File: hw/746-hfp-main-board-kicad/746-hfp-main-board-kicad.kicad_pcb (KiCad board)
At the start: 2 copper layers, 140 x 90 mm, 59 parts, among them J1 5V, J10 Conn_01x01_Socket, J11 Conn_01x01_Socket, J12 Phone_Connector, J13 ESP32_Left_Pins, J14 ESP32_Right_Pins, J15 Power_Connector, J16 Control_board_Connector, J17 Control_board_connector, J18 Conn_01x01_Socket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

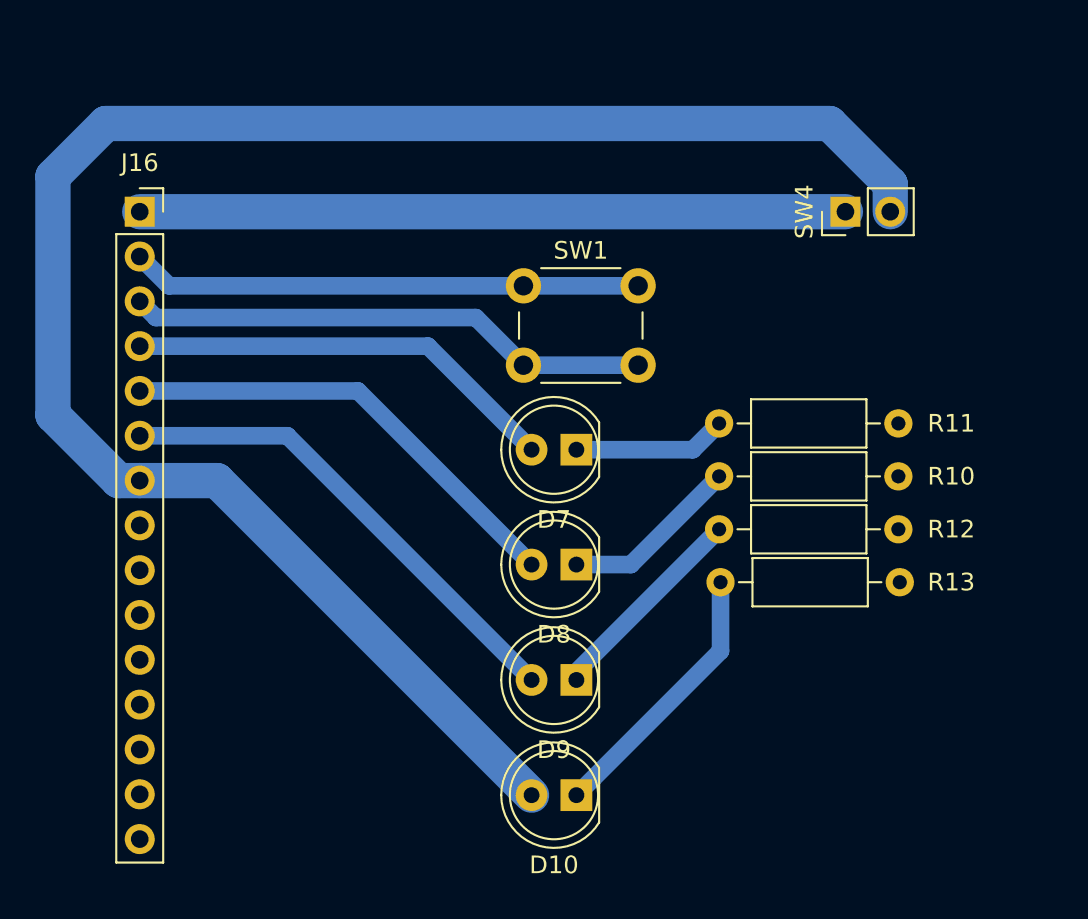
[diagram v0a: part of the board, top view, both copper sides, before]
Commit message: Add schematic & pcb for control board
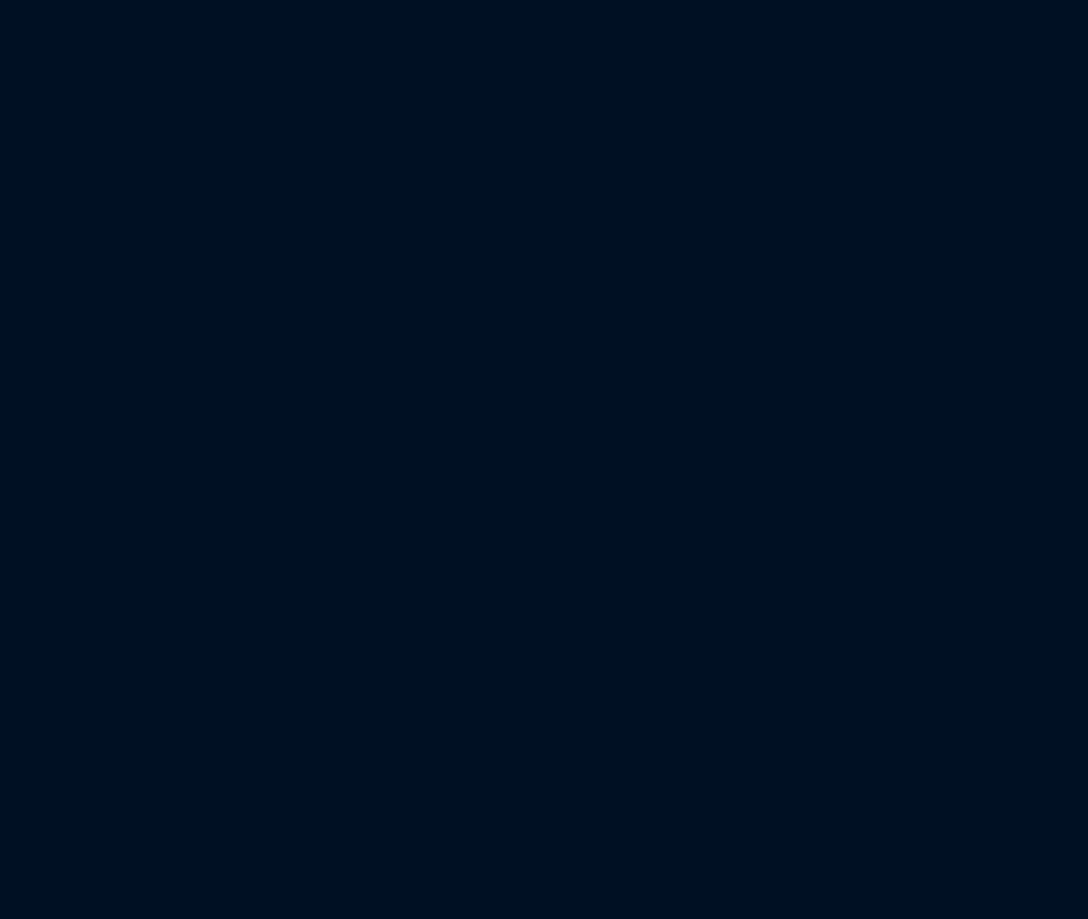
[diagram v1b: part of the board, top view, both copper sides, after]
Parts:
- removed D10, D7, D8, D9: LED, LED_THT:LED_D5.0mm
- removed J16: Control_board_Connector, Connector_PinSocket_2.54mm:PinSocket_1x15_P2.54mm_Vertical
- removed R10, R12: 220, Resistor_THT:R_Axial_DIN0207_L6.3mm_D2.5mm_P10.16mm_Horizontal
- removed R11: 2k, Resistor_THT:R_Axial_DIN0207_L6.3mm_D2.5mm_P10.16mm_Horizontal
- removed R13: 1k, Resistor_THT:R_Axial_DIN0207_L6.3mm_D2.5mm_P10.16mm_Horizontal
- removed SW1: SW_Push, Button_Switch_THT:SW_PUSH_6mm_H5mm
- removed SW4: SW_SPST, Connector_PinHeader_2.54mm:PinHeader_1x02_P2.54mm_Vertical
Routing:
- net +5V: track 276.9 -> 175.6 mm
- net /Control board/+5V_pre_switch: track 40.0 -> 0.00 mm
- net /Control board/ENABLE_PAIRING_BTN (18): track 29.7 -> 0.00 mm
- net /Control board/+3.3V: track 28.9 -> 0.00 mm
- net /Control board/HookSwitchOut (2): track 27.9 -> 0.00 mm
- net /Control board/RingerSignal (16): track 26.3 -> 0.00 mm
- net /Control board/BT_LED_STATE (19): track 24.6 -> 0.00 mm
- net Net-(D10-K): track 15.5 -> 0.00 mm
- net Net-(D9-K): track 11.9 -> 0.00 mm
- net Net-(D8-K): track 10.2 -> 0.00 mm
- net Net-(D7-K): track 8.71 -> 0.00 mm

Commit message: Create kicad pcb
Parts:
- C6: value 2.2nF -> 3.3nF
- J15: footprint Connector_PinHeader_2.54mm:PinHeader_1x02_P2.54mm_Vertical -> Connector_JST:JST_XH_B2B-XH-A_1x02_P2.50mm_Vertical
- R3: value 20k -> 10k
- moved J15 80.5 mm to (145.0, 69.0)
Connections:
- U3 pad 1: +3.3V_Clean -> Net-(U3-REF)
- U3 pad 2: (no net) -> GND
- U3 pad 3: (no net) -> +3.3V_Clean
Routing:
- net GNDA: track 109.4 -> 537.7 mm, vias 2 -> 4
- net +5V: track 175.6 -> 545.8 mm, vias 4 -> 5
- net Mic+: track 12.9 -> 201.7 mm
- net Speaker+: track 11.2 -> 194.0 mm
- net GND: track 0.00 -> 167.9 mm, vias 0 -> 4
- net RingerSignal (16): track 79.8 -> 135.6 mm
- net HookSwitchOut (2): track 25.2 -> 78.1 mm
- net Ringer+: track 9.65 -> 56.5 mm
- net +3.3V_Clean: track 63.8 -> 74.2 mm
- net +3.3V: track 96.2 -> 87.8 mm
- net HookSwitchPower (4): track 23.6 -> 30.2 mm
- net +5V_pre_switch: track 6.24 -> 9.22 mm, vias 1 -> 0
- net Pico_Enable: track 64.1 -> 66.3 mm
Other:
- board text added: "The board is not meant for manufacturing as such some DRC violations have been ignored. Front copper layer is routed only to fool DRC. The actual board is single sided and uses jumper wires acros vias"

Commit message: Improve kicad related
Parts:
- added REF**: PinSocket_1x01_P2.54mm_Vertical, Connector_PinSocket_2.54mm:PinSocket_1x01_P2.54mm_Vertical, F.Cu at (89.0, 29.0)
- added REF**: PinSocket_1x01_P2.54mm_Vertical, Connector_PinSocket_2.54mm:PinSocket_1x01_P2.54mm_Vertical, F.Cu at (95.0, 66.0)
- added REF**: PinSocket_1x01_P2.54mm_Vertical, Connector_PinSocket_2.54mm:PinSocket_1x01_P2.54mm_Vertical, F.Cu at (214.0, 67.0)
- added REF**: PinSocket_1x01_P2.54mm_Vertical, Connector_PinSocket_2.54mm:PinSocket_1x01_P2.54mm_Vertical, F.Cu at (129.0, 63.0)
- added REF**: PinSocket_1x01_P2.54mm_Vertical, Connector_PinSocket_2.54mm:PinSocket_1x01_P2.54mm_Vertical, F.Cu at (142.0, 79.0)
- added REF**: PinSocket_1x01_P2.54mm_Vertical, Connector_PinSocket_2.54mm:PinSocket_1x01_P2.54mm_Vertical, F.Cu at (191.0, 38.0)
- added REF**: PinSocket_1x01_P2.54mm_Vertical, Connector_PinSocket_2.54mm:PinSocket_1x01_P2.54mm_Vertical, F.Cu at (142.0, 74.0)
- added REF**: PinSocket_1x01_P2.54mm_Vertical, Connector_PinSocket_2.54mm:PinSocket_1x01_P2.54mm_Vertical, F.Cu at (115.0, 32.0)
- added REF**: PinSocket_1x01_P2.54mm_Vertical, Connector_PinSocket_2.54mm:PinSocket_1x01_P2.54mm_Vertical, F.Cu at (108.0, 41.0)
- added REF**: PinSocket_1x01_P2.54mm_Vertical, Connector_PinSocket_2.54mm:PinSocket_1x01_P2.54mm_Vertical, F.Cu at (150.0, 88.0)
- added REF**: PinSocket_1x01_P2.54mm_Vertical, Connector_PinSocket_2.54mm:PinSocket_1x01_P2.54mm_Vertical, F.Cu at (195.0, 30.0)
- added REF**: PinSocket_1x01_P2.54mm_Vertical, Connector_PinSocket_2.54mm:PinSocket_1x01_P2.54mm_Vertical, F.Cu at (192.0, 83.0)
- added REF**: PinSocket_1x01_P2.54mm_Vertical, Connector_PinSocket_2.54mm:PinSocket_1x01_P2.54mm_Vertical, F.Cu at (151.0, 66.0)
- added REF**: PinSocket_1x01_P2.54mm_Vertical, Connector_PinSocket_2.54mm:PinSocket_1x01_P2.54mm_Vertical, F.Cu at (156.0, 23.0)
- added REF**: PinSocket_1x01_P2.54mm_Vertical, Connector_PinSocket_2.54mm:PinSocket_1x01_P2.54mm_Vertical, F.Cu at (163.0, 106.0)
- added REF**: PinSocket_1x01_P2.54mm_Vertical, Connector_PinSocket_2.54mm:PinSocket_1x01_P2.54mm_Vertical, F.Cu at (113.0, 25.0)
- added REF**: PinSocket_1x01_P2.54mm_Vertical, Connector_PinSocket_2.54mm:PinSocket_1x01_P2.54mm_Vertical, F.Cu at (94.0, 43.0)
- added REF**: PinSocket_1x01_P2.54mm_Vertical, Connector_PinSocket_2.54mm:PinSocket_1x01_P2.54mm_Vertical, F.Cu at (171.0, 85.0)
- added REF**: PinSocket_1x01_P2.54mm_Vertical, Connector_PinSocket_2.54mm:PinSocket_1x01_P2.54mm_Vertical, F.Cu at (83.0, 30.0)
- added REF**: PinSocket_1x01_P2.54mm_Vertical, Connector_PinSocket_2.54mm:PinSocket_1x01_P2.54mm_Vertical, F.Cu at (102.0, 68.0)
- added REF**: PinSocket_1x01_P2.54mm_Vertical, Connector_PinSocket_2.54mm:PinSocket_1x01_P2.54mm_Vertical, F.Cu at (94.0, 38.0)
- added REF**: PinSocket_1x01_P2.54mm_Vertical, Connector_PinSocket_2.54mm:PinSocket_1x01_P2.54mm_Vertical, F.Cu at (116.0, 28.0)
- added REF**: PinSocket_1x01_P2.54mm_Vertical, Connector_PinSocket_2.54mm:PinSocket_1x01_P2.54mm_Vertical, F.Cu at (199.0, 59.0)
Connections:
- J12 pad 6: Dialer (15) -> HookSwitchOut (2)
- J14 pad 13: Dialer (15) -> HookSwitchOut (2)
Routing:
- net HookSwitchOut (2): track 78.1 -> 106.0 mm, vias 2 -> 0
- net Dialer (15): track 26.8 -> 0.00 mm
- net GND: track 167.9 -> 164.2 mm, vias 4 -> 0
- net RingerSignal (16): track 135.6 -> 138.4 mm, vias 2 -> 0
- net BT_LED_STATE (19): track 34.9 -> 37.0 mm
- net GNDA: track 537.7 -> 535.6 mm, vias 4 -> 0
- net ENABLE_PAIRING_BTN (18): track 35.2 -> 37.0 mm
- net +5V: track 545.8 -> 544.1 mm, vias 5 -> 0
- net Ringer+: track 56.5 -> 56.9 mm, vias 2 -> 0
- net Mic+: track 201.7 -> 201.6 mm, vias 2 -> 0
- net Speaker+: track 194.0 -> 193.9 mm, vias 2 -> 0
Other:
- board text added: "BUG: The spacing between the ESP32 pin rows is about 1.5mm smaller than it should. If you're planning to use this board, increase the spacing between J13 and J14"

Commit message: Fixed pcb
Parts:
- Q1: footprint Package_TO_SOT_THT:TO-220-3_Vertical -> Package_TO_SOT_THT:TO-92
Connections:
- J12 pad 6: HookSwitchOut (2) -> Dialer(15)
- J14 pad 13: HookSwitchOut (2) -> Dialer(15)
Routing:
- net Dialer(15): track 0.00 -> 27.2 mm
- net HookSwitchOut (2): track 106.0 -> 78.9 mm
- net GND: track 164.2 -> 175.9 mm
- net RingerEnabled (17): track 56.7 -> 61.3 mm
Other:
- board text added: "BUG: The spacing between the ESP32 pin rows is about 1.5mm smaller than it should be. If you're planning to use this board, increase the spacing between J13 and J14"
- board text removed: "BUG: The spacing between the ESP32 pin rows is about 1.5mm smaller than it should. If you're planning to use this board, increase the spacing between J13 and J14"

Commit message: Fixed board
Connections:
- net Dialer(15) renamed Dialer (15)
- J13 pad 10: unconnected-(J13-Pin_10-Pad10) -> Audio_SCL (27)
- J13 pad 8: Audio_SCL (27) -> unconnected-(J13-Pin_8-Pad8)
- U3 pad 1: Net-(U3-REF) -> +3.3V_Clean
- U3 pad 2: GND -> (no net)
- U3 pad 3: +3.3V_Clean -> (no net)
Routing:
- net Audio_SCL (27): track 31.8 -> 38.7 mm, vias 0 -> 2
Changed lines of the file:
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@@
   (net 24 "unconnected-(J13-Pin_7-Pad7)")
   (net 25 "Audio_SDA (26)")
-  (net 26 "unconnected-(J13-Pin_10-Pad10)")
+  (net 26 "Dialer (15)")
   (net 27 "unconnected-(J13-Pin_12-Pad12)")
   (net 28 "unconnected-(J13-Pin_13-Pad13)")
@@
   (net 75 "unconnected-(J13-Pin_11-Pad11)")
   (net 76 "Net-(U3-REF)")
-  (net 77 "Dialer(15)")
+  (net 77 "unconnected-(J13-Pin_8-Pad8)")
   (footprint "Connector_JST:JST_XH_B2B-XH-A_1x02_P2.50mm_Vertical" (layer "F.Cu")
     (at 145 69 90)
@@
       (stroke (width 0.1) (type solid)) (layer "F.Fab"))
     (pad "1" thru_hole rect (at 0 0 180) (size 1.5 1.5) (drill 0.8) (layers "*.Cu" "*.Mask")
-      (net 76 "Net-(U3-REF)") (pinfunction "K") (pintype "passive"))
-    (pad "2" thru_hole circle (at 2.54 0 180) (size 1.5 1.5) (drill 0.8) (layers "*.Cu" "*.Mask")
-      (net 1 "GND"))
-    (pad "3" thru_hole circle (at 5.08 0 180) (size 1.5 1.5) (drill 0.8) (layers "*.Cu" "*.Mask")
-      (net 43 "+3.3V_Clean"))
+      (net 43 "+3.3V_Clean") (pinfunction "K") (pintype "passive"))
+    (pad "2" thru_hole circle (at 2.54 0 180) (size 1.5 1.5) (drill 0.8) (layers "*.Cu" "*.Mask"))
+    (pad "3" thru_hole circle (at 5.08 0 180) (size 1.5 1.5) (drill 0.8) (layers "*.Cu" "*.Mask"))
     (model "${KICAD6_3DMODEL_DIR}/Package_TO_SOT_THT.3dshapes/TO-92_Inline_Wide.wrl"
       (offset (xyz 0 0 0))
@@
       (net 24 "unconnected-(J13-Pin_7-Pad7)") (pinfunction "Pin_7") (pintype "passive"))
     (pad "8" thru_hole oval (at 0 17.78 180) (size 1.7 1.7) (drill 1) (layers "*.Cu" "*.Mask")
-      (net 74 "Audio_SCL (27)") (pinfunction "Pin_8") (pintype "passive"))
+      (net 77 "unconnected-(J13-Pin_8-Pad8)") (pinfunction "Pin_8") (pintype "passive"))
     (pad "9" thru_hole oval (at 0 20.32 180) (size 1.7 1.7) (drill 1) (layers "*.Cu" "*.Mask")
       (net 25 "Audio_SDA (26)") (pinfunction "Pin_9") (pintype "passive"))
     (pad "10" thru_hole oval (at 0 22.86 180) (size 1.7 1.7) (drill 1) (layers "*.Cu" "*.Mask")
-      (net 26 "unconnected-(J13-Pin_10-Pad10)") (pinfunction "Pin_10") (pintype "passive"))
+      (net 74 "Audio_SCL (27)") (pinfunction "Pin_10") (pintype "passive"))
     (pad "11" thru_hole oval (at 0 25.4 180) (size 1.7 1.7) (drill 1) (layers "*.Cu" "*.Mask")
       (net 75 "unconnected-(J13-Pin_11-Pad11)") (pinfunction "Pin_11") (pintype "passive"))
@@
       (net 40 "HookSwitchOut (2)") (pinfunction "Pin_12") (pintype "passive"))
     (pad "13" thru_hole oval (at 0 30.48 180) (size 1.7 1.7) (drill 1) (layers "*.Cu" "*.Mask")
-      (net 77 "Dialer(15)") (pinfunction "Pin_13") (pintype "passive"))
+      (net 26 "Dialer (15)") (pinfunction "Pin_13") (pintype "passive"))
     (pad "14" thru_hole oval (at 0 33.02 180) (size 1.7 1.7) (drill 1) (layers "*.Cu" "*.Mask")
       (net 1 "GND") (pinfunction "Pin_14") (pintype "passive"))
@@
       (net 41 "+3.3V") (pinfunction "Pin_5") (pintype "passive"))
     (pad "6" thru_hole oval (at 0 12.7 90) (size 1.7 1.7) (drill 1) (layers "*.Cu" "*.Mask")
-      (net 77 "Dialer(15)") (pinfunction "Pin_6") (pintype "passive"))
+      (net 26 "Dialer (15)") (pinfunction "Pin_6") (pintype "passive"))
     (pad "7" thru_hole oval (at 0 15.24 90) (size 1.7 1.7) (drill 1) (layers "*.Cu" "*.Mask")
       (net 1 "GND") (pinfunction "Pin_7") (pintype "passive"))
@@
   (segment (start 165.11 59.94) (end 163 57.83) (width 1) (layer "B.Cu") (net 25))
   (segment (start 163 57.83) (end 163 56.65) (width 1) (layer "B.Cu") (net 25))
+  (segment (start 113 27.8) (end 102.9 27.8) (width 1) (layer "B.Cu") (net 26))
+  (segment (start 120.1 26.45) (end 114.35 26.45) (width 1) (layer "B.Cu") (net 26))
+  (segment (start 114.35 26.45) (end 113 27.8) (width 1) (layer "B.Cu") (net 26))
+  (segment (start 102.9 27.8) (end 96.7 34) (width 1) (layer "B.Cu") (net 26))
+  (segment (start 120.57 26.92) (end 120.1 26.45) (width 1) (layer "B.Cu") (net 26))
   (segment (start 137 72) (end 132 72) (width 1) (layer "B.Cu") (net 34))
   (segment (start 125 65) (end 125 49.13) (width 1) (layer "B.Cu") (net 34))
@@
   (segment (start 103 63) (end 112 63) (width 1) (layer "B.Cu") (net 45))
   (segment (start 193.74 92.74) (end 193.74 95.28) (width 1) (layer "B.Cu") (net 71))
-  (segment (start 161 57.19) (end 143.43 39.62) (width 1) (layer "B.Cu") (net 74))
-  (segment (start 161 58.37) (end 161 57.19) (width 1) (layer "B.Cu") (net 74))
+  (segment (start 147 43) (end 147 35) (width 1) (layer "F.Cu") (net 74))
+  (via (at 147 43) (size 1) (drill 0.7) (layers "F.Cu" "B.Cu") (free) (net 74))
+  (via (at 147 35) (size 1) (drill 0.7) (layers "F.Cu" "B.Cu") (free) (net 74))
+  (segment (start 161 57) (end 147 43) (width 1) (layer "B.Cu") (net 74))
+  (segment (start 143.89 35) (end 143.43 34.54) (width 1) (layer "B.Cu") (net 74))
+  (segment (start 161 58.37) (end 161 57) (width 1) (layer "B.Cu") (net 74))
   (segment (start 165.11 62.48) (end 161 58.37) (width 1) (layer "B.Cu") (net 74))
+  (segment (start 147 35) (end 143.89 35) (width 1) (layer "B.Cu") (net 74))
   (segment (start 203.46 38.46) (end 209 44) (width 1) (layer "B.Cu") (net 76))
   (segment (start 209 44) (end 209 50) (width 1) (layer "B.Cu") (net 76))
   (segment (start 199 38.46) (end 203.46 38.46) (width 1) (layer "B.Cu") (net 76))
-  (segment (start 113 27.8) (end 102.9 27.8) (width 1) (layer "B.Cu") (net 77))
-  (segment (start 120.1 26.45) (end 114.35 26.45) (width 1) (layer "B.Cu") (net 77))
-  (segment (start 114.35 26.45) (end 113 27.8) (width 1) (layer "B.Cu") (net 77))
-  (segment (start 102.9 27.8) (end 96.7 34) (width 1) (layer "B.Cu") (net 77))
-  (segment (start 120.57 26.92) (end 120.1 26.45) (width 1) (layer "B.Cu") (net 77))
   (zone (net 1) (net_name "GND") (layer "B.Cu") (hatch edge 0.5)
     (connect_pads (clearance 0.5))
